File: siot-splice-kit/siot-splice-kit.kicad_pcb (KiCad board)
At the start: 2 copper layers, 40.6 x 46.6 mm, 2 parts, among them J1 xConnect_smd, J2 Screw_Terminal_5mm_01x03

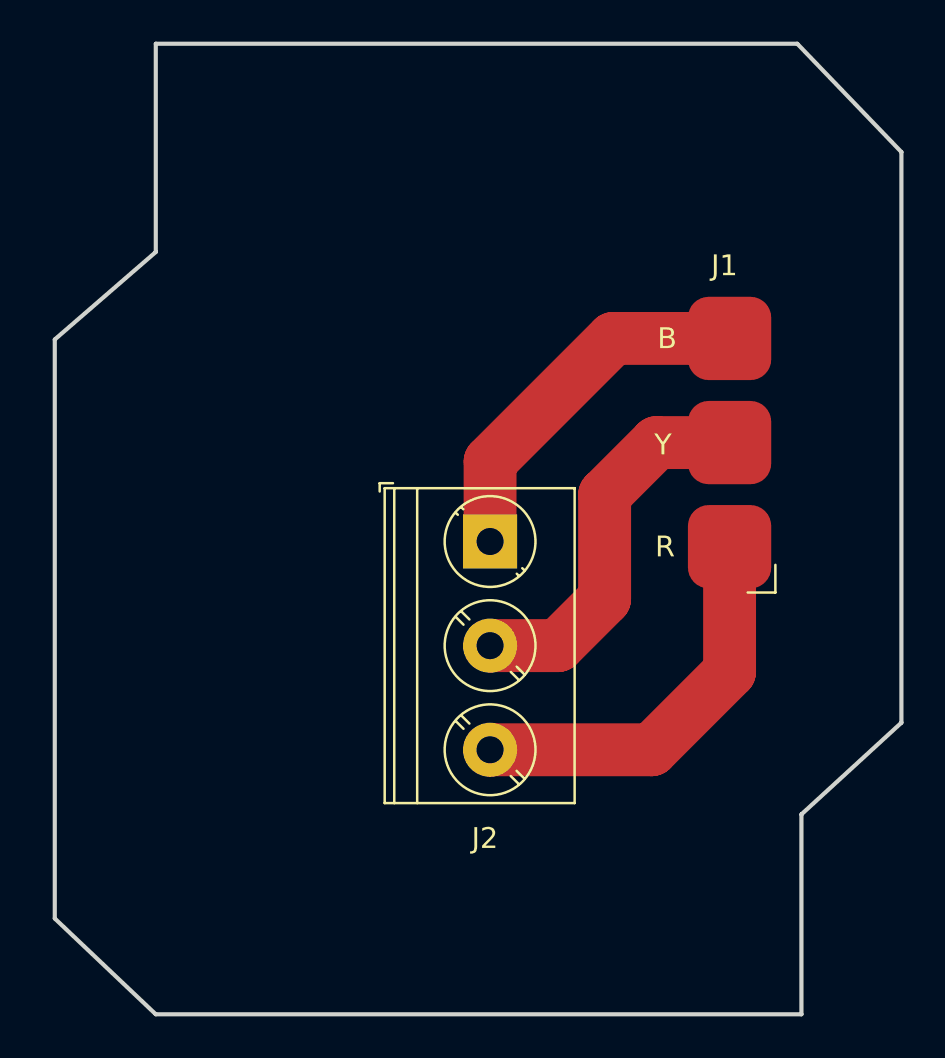
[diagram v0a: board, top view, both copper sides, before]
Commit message: updates for relay/splice kit
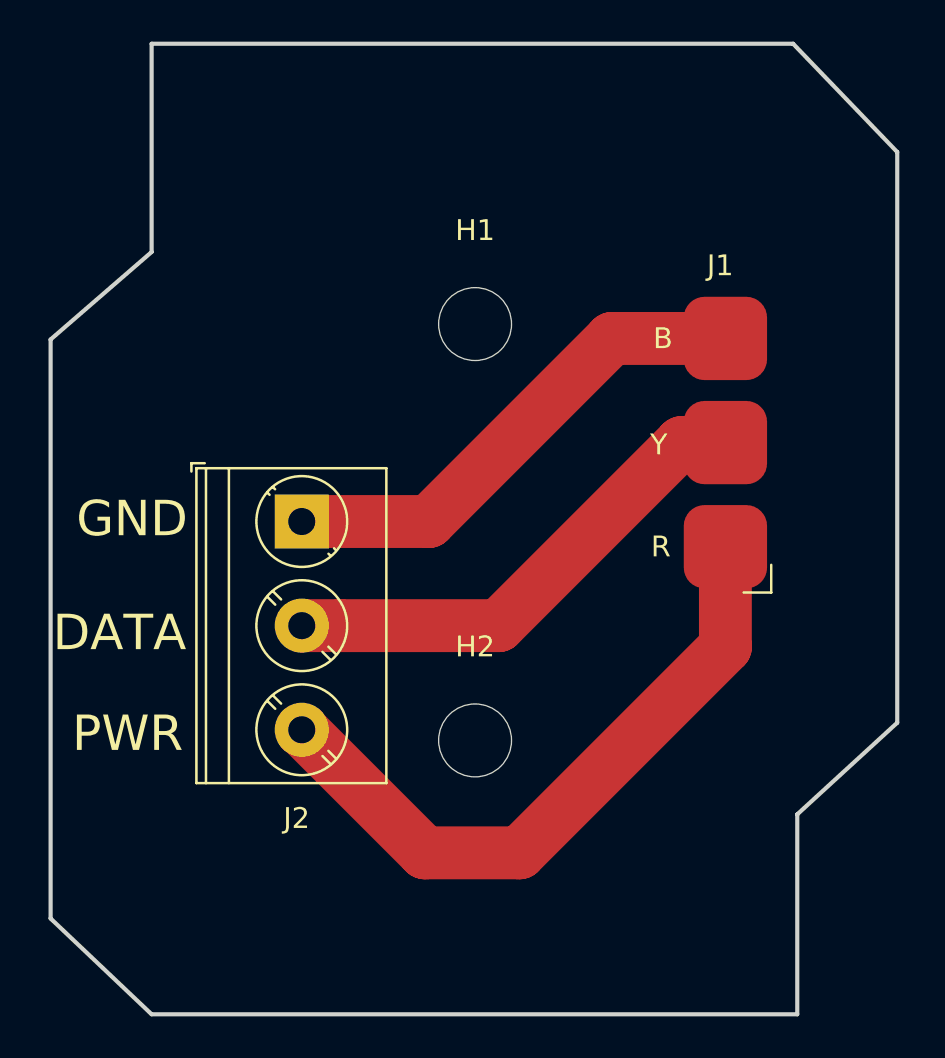
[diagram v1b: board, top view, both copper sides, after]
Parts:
- added H1: MountingHole, MountingHole:MountingHole_3.5mm, F.Cu at (80.3, 75.6)
- added H2: MountingHole, MountingHole:MountingHole_3.5mm, F.Cu at (80.3, 95.5)
- moved J2 9.09 mm to (72.0, 85.0)
- moved J1 0.20 mm to (92.3, 86.2)
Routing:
- net Net-(J1-PadR): track 19.1 -> 31.7 mm
- net Net-(J1-PadB): track 17.8 -> 24.0 mm
- net Net-(J1-PadY): track 18.5 -> 24.0 mm
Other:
- board text added: "DATA"
- board text added: "GND"
- board text added: "PWR"
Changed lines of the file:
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@@
   (general
     (thickness 1.6)
-    (drawings 10)
+    (drawings 35)
     (tracks 11)
     (zones 0)
-    (modules 2)
+    (modules 4)
     (nets 4)
   )
@@
       (outputformat 1)
       (mirror false)
-      (drillshape 1)
+      (drillshape 0)
       (scaleselection 1)
-      (outputdirectory ""))
+      (outputdirectory "mfg/"))
   )
   (net 0 "")
@@
     (add_net "Net-(J1-PadY)")
   )
+  (module MountingHole:MountingHole_3.5mm (layer F.Cu)
+    (at 80.28 95.55)
+    (descr "Mounting Hole 3.5mm, no annular")
+    (tags "mounting hole 3.5mm no annular")
+    (attr virtual)
+    (fp_text reference H2 (at 0 -4.5) (layer F.SilkS)
+      (effects (font (size 1 1) (thickness 0.15)))
+    )
+    (fp_text value MountingHole (at 0 4.5) (layer F.Fab)
+      (effects (font (size 1 1) (thickness 0.15)))
+    )
+    (fp_circle (center 0 0) (end 3.75 0) (layer F.CrtYd) (width 0.05))
+    (fp_circle (center 0 0) (end 3.5 0) (layer Cmts.User) (width 0.15))
+    (fp_text user %R (at 0.3 0) (layer F.Fab)
+      (effects (font (size 1 1) (thickness 0.15)))
+    )
+    (pad 1 np_thru_hole circle (at 0 0) (size 3.5 3.5) (drill 3.5) (layers *.Cu *.Mask))
+  )
+  (module MountingHole:MountingHole_3.5mm (layer F.Cu)
+    (at 80.28 75.56)
+    (descr "Mounting Hole 3.5mm, no annular")
+    (tags "mounting hole 3.5mm no annular")
+    (attr virtual)
+    (fp_text reference H1 (at 0 -4.5) (layer F.SilkS)
+      (effects (font (size 1 1) (thickness 0.15)))
+    )
+    (fp_text value MountingHole (at 0 4.5) (layer F.Fab)
+      (effects (font (size 1 1) (thickness 0.15)))
+    )
+    (fp_circle (center 0 0) (end 3.75 0) (layer F.CrtYd) (width 0.05))
+    (fp_circle (center 0 0) (end 3.5 0) (layer Cmts.User) (width 0.15))
+    (fp_text user %R (at 0.3 0) (layer F.Fab)
+      (effects (font (size 1 1) (thickness 0.15)))
+    )
+    (pad 1 np_thru_hole circle (at 0 0) (size 3.5 3.5) (drill 3.5) (layers *.Cu *.Mask))
+  )
   (module TerminalBlock_Phoenix:TerminalBlock_Phoenix_PT-1,5-3-5.0-H_1x03_P5.00mm_Horizontal (layer F.Cu)
-    (at 81 86 270)
+    (at 71.96 85.04 270)
     (descr "Terminal Block Phoenix PT-1,5-3-5.0-H, 3 pins, pitch 5mm, size 15x9mm^2, drill diamater 1.3mm, pad diameter 2.6mm, see http://www.mouser.com/ds/2/324/ItemDetail_1935161-922578.pdf, script-generated using https://github.com/pointhi/kicad-footprint-generator/scripts/TerminalBlock_Phoenix")
     (tags "THT Terminal Block Phoenix PT-1,5-3-5.0-H pitch 5mm size 15x9mm^2 drill 1.3mm pad 2.6mm")
@@
   )
   (module BEC:xConnect_smd (layer F.Cu)
-    (at 92.5 86.25 180)
+    (at 92.3 86.25 180)
     (descr "mounting holes for xConnect connector")
     (tags "Through hole 1x03 single row")
@@
     )
   )
-  (gr_line (start 100.75 94.7) (end 100.75 67.3) (layer Edge.Cuts) (width 0.2))
-  (gr_line (start 64.95 108.7) (end 95.95 108.7) (layer Edge.Cuts) (width 0.2))
-  (gr_line (start 60.1 76.3) (end 60.1 104.1) (layer Edge.Cuts) (width 0.2))
-  (gr_line (start 95.75 62.1) (end 64.95 62.1) (layer Edge.Cuts) (width 0.2))
-  (gr_line (start 95.75 62.1) (end 100.75 67.3) (layer Edge.Cuts) (width 0.2))
-  (gr_line (start 64.95 62.1) (end 64.95 72.1) (layer Edge.Cuts) (width 0.2))
-  (gr_line (start 64.95 72.1) (end 60.1 76.3) (layer Edge.Cuts) (width 0.2))
-  (gr_line (start 60.1 104.1) (end 64.95 108.7) (layer Edge.Cuts) (width 0.2))
-  (gr_line (start 95.95 108.7) (end 95.95 99.1) (layer Edge.Cuts) (width 0.2))
-  (gr_line (start 95.95 99.1) (end 100.75 94.7) (layer Edge.Cuts) (width 0.2))
-  (segment (start 81 82.16) (end 86.91 76.25) (width 2.54) (layer F.Cu) (net 1))
-  (segment (start 81 86) (end 81 82.16) (width 2.54) (layer F.Cu) (net 1))
-  (segment (start 86.91 76.25) (end 92.5 76.25) (width 2.54) (layer F.Cu) (net 1))
-  (segment (start 81 91) (end 84.25 91) (width 2.54) (layer F.Cu) (net 2))
-  (segment (start 84.25 91) (end 86.5 88.75) (width 2.54) (layer F.Cu) (net 2))
-  (segment (start 86.5 88.75) (end 86.5 83.75) (width 2.54) (layer F.Cu) (net 2))
-  (segment (start 89 81.25) (end 92.5 81.25) (width 2.54) (layer F.Cu) (net 2))
-  (segment (start 86.5 83.75) (end 89 81.25) (width 2.54) (layer F.Cu) (net 2))
-  (segment (start 92.5 92.25) (end 92.5 86.25) (width 2.54) (layer F.Cu) (net 3))
-  (segment (start 81 96) (end 88.75 96) (width 2.54) (layer F.Cu) (net 3))
-  (segment (start 88.75 96) (end 92.5 92.25) (width 2.54) (layer F.Cu) (net 3))
+  (gr_line (start 30.969479 90.248889) (end 30.969479 65.748888) (layer Dwgs.User) (width 0.2))
+  (gr_arc (start 28.875555 56.748889) (end 21.96948 56.748889) (angle -90) (layer Dwgs.User) (width 0.2))
+  (gr_circle (center 5.875555 72.748889) (end 7.590055 72.748889) (layer Dwgs.User) (width 0.2))
+  (gr_arc (start 28.875555 90.248889) (end 28.875555 92.342814) (angle -90) (layer Dwgs.User) (width 0.2))
+  (gr_arc (start 28.875555 99.748889) (end 28.875555 92.342814) (angle -90) (layer Dwgs.User) (width 0.2))
+  (gr_circle (center 5.875555 92.748889) (end 7.590055 92.748889) (layer Dwgs.User) (width 0.2))
+  (gr_line (start 19.875555 54.654965) (end -7.624445 54.654965) (layer Dwgs.User) (width 0.2))
+  (gr_arc (start 19.875555 56.748889) (end 21.96948 56.748889) (angle -90) (layer Dwgs.User) (width 0.2))
+  (gr_line (start 21.46948 108.74889) (end 21.46948 99.74889) (layer Dwgs.User) (width 0.2))
+  (gr_arc (start 19.375555 108.748889) (end 19.375555 110.842814) (angle -90) (layer Dwgs.User) (width 0.2))
+  (gr_line (start -8.124445 110.842814) (end 19.375555 110.842814) (layer Dwgs.User) (width 0.2))
+  (gr_arc (start -17.124445 99.748889) (end -19.21837 99.748889) (angle -90) (layer Dwgs.User) (width 0.2))
+  (gr_line (start -19.218369 75.24889) (end -19.218369 99.74889) (layer Dwgs.User) (width 0.2))
+  (gr_arc (start 28.875555 65.748889) (end 30.96948 65.748889) (angle -90) (layer Dwgs.User) (width 0.2))
+  (gr_line (start -9.71837 56.748889) (end -9.71837 65.748888) (layer Dwgs.User) (width 0.2))
+  (gr_arc (start -7.624445 56.748889) (end -7.624445 54.654965) (angle -90) (layer Dwgs.User) (width 0.2))
+  (gr_arc (start -17.124445 75.248889) (end -17.124445 73.154965) (angle -90) (layer Dwgs.User) (width 0.2))
+  (gr_arc (start -17.124445 108.748889) (end -10.21837 108.748889) (angle -90) (layer Dwgs.User) (width 0.2))
+  (gr_arc (start -17.124445 65.748889) (end -17.124445 73.154965) (angle -90) (layer Dwgs.User) (width 0.2))
+  (gr_arc (start -8.124445 108.748889) (end -10.21837 108.748889) (angle -90) (layer Dwgs.User) (width 0.2))
+  (gr_circle (center 80.275555 75.548889) (end 81.990055 75.548889) (layer Dwgs.User) (width 0.2))
+  (gr_circle (center 80.275555 95.548889) (end 81.990055 95.548889) (layer Dwgs.User) (width 0.2))
+  (gr_text PWR (at 63.6 95.22) (layer F.SilkS)
+    (effects (font (size 1.7 1.7) (thickness 0.25)))
+  )
+  (gr_text DATA (at 63.21 90.38) (layer F.SilkS)
+    (effects (font (size 1.7 1.7) (thickness 0.25)))
+  )
+  (gr_text GND (at 63.81 84.91) (layer F.SilkS)
+    (effects (font (size 1.7 1.7) (thickness 0.25)))
+  )
+  (gr_line (start 100.55 94.7) (end 100.55 67.3) (layer Edge.Cuts) (width 0.2))
+  (gr_line (start 64.75 108.7) (end 95.75 108.7) (layer Edge.Cuts) (width 0.2))
+  (gr_line (start 59.9 76.3) (end 59.9 104.1) (layer Edge.Cuts) (width 0.2))
+  (gr_line (start 95.55 62.1) (end 64.75 62.1) (layer Edge.Cuts) (width 0.2))
+  (gr_line (start 95.55 62.1) (end 100.55 67.3) (layer Edge.Cuts) (width 0.2))
+  (gr_line (start 64.75 62.1) (end 64.75 72.1) (layer Edge.Cuts) (width 0.2))
+  (gr_line (start 64.75 72.1) (end 59.9 76.3) (layer Edge.Cuts) (width 0.2))
+  (gr_line (start 59.9 104.1) (end 64.75 108.7) (layer Edge.Cuts) (width 0.2))
+  (gr_line (start 95.75 108.7) (end 95.75 99.1) (layer Edge.Cuts) (width 0.2))
+  (gr_line (start 95.75 99.1) (end 100.55 94.7) (layer Edge.Cuts) (width 0.2))
+  (segment (start 78.06 85.04) (end 71.96 85.04) (width 2.54) (layer F.Cu) (net 1))
+  (segment (start 92.3 76.25) (end 86.85 76.25) (width 2.54) (layer F.Cu) (net 1))
+  (segment (start 86.85 76.25) (end 78.06 85.04) (width 2.54) (layer F.Cu) (net 1))
+  (segment (start 73.798477 90.04) (end 71.96 90.04) (width 2.54) (layer F.Cu) (net 2))
+  (segment (start 81.41 90.04) (end 73.798477 90.04) (width 2.54) (layer F.Cu) (net 2))
+  (segment (start 90.2 81.25) (end 81.41 90.04) (width 2.54) (layer F.Cu) (net 2))
+  (segment (start 92.3 81.25) (end 90.2 81.25) (width 2.54) (layer F.Cu) (net 2))
+  (segment (start 92.3 86.25) (end 92.3 91.06) (width 2.54) (layer F.Cu) (net 3))
+  (segment (start 92.3 91.06) (end 82.41 100.95) (width 2.54) (layer F.Cu) (net 3))
+  (segment (start 77.87 100.95) (end 71.96 95.04) (width 2.54) (layer F.Cu) (net 3))
+  (segment (start 82.41 100.95) (end 77.87 100.95) (width 2.54) (layer F.Cu) (net 3))
 )

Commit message: updates
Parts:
- moved J2 20.0 mm to (90.6, 92.2)
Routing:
- net Net-(J1-PadR): track 31.7 -> 18.1 mm
- net Net-(J1-PadB): track 24.0 -> 20.9 mm
- net Net-(J1-PadY): track 24.0 -> 23.4 mm, vias 0 -> 1
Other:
- board size 40.6 x 46.6 mm -> 37.3 x 46.6 mm
- board text added: "SIOT Splice Kit v2"
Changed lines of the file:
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@@
   (general
     (thickness 1.6)
-    (drawings 35)
-    (tracks 11)
+    (drawings 36)
+    (tracks 14)
     (zones 0)
     (modules 4)
@@
     (via_min_size 0.4)
     (via_min_drill 0.3)
+    (user_via 2.286 1.016)
     (uvia_size 0.3)
     (uvia_drill 0.1)
@@
   )
   (module TerminalBlock_Phoenix:TerminalBlock_Phoenix_PT-1,5-3-5.0-H_1x03_P5.00mm_Horizontal (layer F.Cu)
-    (at 71.96 85.04 270)
+    (at 90.6 92.2 270)
     (descr "Terminal Block Phoenix PT-1,5-3-5.0-H, 3 pins, pitch 5mm, size 15x9mm^2, drill diamater 1.3mm, pad diameter 2.6mm, see http://www.mouser.com/ds/2/324/ItemDetail_1935161-922578.pdf, script-generated using https://github.com/pointhi/kicad-footprint-generator/scripts/TerminalBlock_Phoenix")
     (tags "THT Terminal Block Phoenix PT-1,5-3-5.0-H pitch 5mm size 15x9mm^2 drill 1.3mm pad 2.6mm")
@@
     )
   )
+  (gr_text "SIOT Splice Kit v2" (at 81 65.2) (layer F.SilkS)
+    (effects (font (size 2 2) (thickness 0.3)))
+  )
   (gr_line (start 30.969479 90.248889) (end 30.969479 65.748888) (layer Dwgs.User) (width 0.2))
   (gr_arc (start 28.875555 56.748889) (end 21.96948 56.748889) (angle -90) (layer Dwgs.User) (width 0.2))
@@
   (gr_circle (center 80.275555 75.548889) (end 81.990055 75.548889) (layer Dwgs.User) (width 0.2))
   (gr_circle (center 80.275555 95.548889) (end 81.990055 95.548889) (layer Dwgs.User) (width 0.2))
-  (gr_text PWR (at 63.6 95.22) (layer F.SilkS)
+  (gr_text PWR (at 72.4 101.6) (layer F.SilkS)
     (effects (font (size 1.7 1.7) (thickness 0.25)))
   )
-  (gr_text DATA (at 63.21 90.38) (layer F.SilkS)
+  (gr_text DATA (at 72.4 96.6) (layer F.SilkS)
     (effects (font (size 1.7 1.7) (thickness 0.25)))
   )
-  (gr_text GND (at 63.81 84.91) (layer F.SilkS)
+  (gr_text GND (at 72.6 92.2) (layer F.SilkS)
     (effects (font (size 1.7 1.7) (thickness 0.25)))
   )
-  (gr_line (start 100.55 94.7) (end 100.55 67.3) (layer Edge.Cuts) (width 0.2))
+  (gr_line (start 98.9 94.7) (end 98.9 67.3) (layer Edge.Cuts) (width 0.2))
   (gr_line (start 64.75 108.7) (end 95.75 108.7) (layer Edge.Cuts) (width 0.2))
-  (gr_line (start 59.9 76.3) (end 59.9 104.1) (layer Edge.Cuts) (width 0.2))
+  (gr_line (start 61.6 76.3) (end 61.6 104.1) (layer Edge.Cuts) (width 0.2))
   (gr_line (start 95.55 62.1) (end 64.75 62.1) (layer Edge.Cuts) (width 0.2))
-  (gr_line (start 95.55 62.1) (end 100.55 67.3) (layer Edge.Cuts) (width 0.2))
+  (gr_line (start 95.55 62.1) (end 98.9 67.3) (layer Edge.Cuts) (width 0.2))
   (gr_line (start 64.75 62.1) (end 64.75 72.1) (layer Edge.Cuts) (width 0.2))
-  (gr_line (start 64.75 72.1) (end 59.9 76.3) (layer Edge.Cuts) (width 0.2))
-  (gr_line (start 59.9 104.1) (end 64.75 108.7) (layer Edge.Cuts) (width 0.2))
+  (gr_line (start 64.75 72.1) (end 61.6 76.3) (layer Edge.Cuts) (width 0.2))
+  (gr_line (start 61.6 104.1) (end 64.75 108.7) (layer Edge.Cuts) (width 0.2))
   (gr_line (start 95.75 108.7) (end 95.75 99.1) (layer Edge.Cuts) (width 0.2))
-  (gr_line (start 95.75 99.1) (end 100.55 94.7) (layer Edge.Cuts) (width 0.2))
-  (segment (start 78.06 85.04) (end 71.96 85.04) (width 2.54) (layer F.Cu) (net 1))
-  (segment (start 92.3 76.25) (end 86.85 76.25) (width 2.54) (layer F.Cu) (net 1))
-  (segment (start 86.85 76.25) (end 78.06 85.04) (width 2.54) (layer F.Cu) (net 1))
-  (segment (start 73.798477 90.04) (end 71.96 90.04) (width 2.54) (layer F.Cu) (net 2))
-  (segment (start 81.41 90.04) (end 73.798477 90.04) (width 2.54) (layer F.Cu) (net 2))
-  (segment (start 90.2 81.25) (end 81.41 90.04) (width 2.54) (layer F.Cu) (net 2))
-  (segment (start 92.3 81.25) (end 90.2 81.25) (width 2.54) (layer F.Cu) (net 2))
-  (segment (start 92.3 86.25) (end 92.3 91.06) (width 2.54) (layer F.Cu) (net 3))
-  (segment (start 92.3 91.06) (end 82.41 100.95) (width 2.54) (layer F.Cu) (net 3))
-  (segment (start 77.87 100.95) (end 71.96 95.04) (width 2.54) (layer F.Cu) (net 3))
-  (segment (start 82.41 100.95) (end 77.87 100.95) (width 2.54) (layer F.Cu) (net 3))
+  (gr_line (start 95.75 99.1) (end 98.9 94.7) (layer Edge.Cuts) (width 0.2))
+  (segment (start 90.2 76.25) (end 87 79.45) (width 2.54) (layer F.Cu) (net 1))
+  (segment (start 92.3 76.25) (end 90.2 76.25) (width 2.54) (layer F.Cu) (net 1))
+  (segment (start 87 88.6) (end 90.6 92.2) (width 2.54) (layer F.Cu) (net 1))
+  (segment (start 87 79.45) (end 87 88.6) (width 2.54) (layer F.Cu) (net 1))
+  (via (at 96.1 81.2) (size 2.286) (drill 1.016) (layers F.Cu B.Cu) (net 2))
+  (segment (start 92.3 81.25) (end 96.05 81.25) (width 2.54) (layer F.Cu) (net 2))
+  (segment (start 96.05 81.25) (end 96.1 81.2) (width 2.54) (layer F.Cu) (net 2))
+  (segment (start 96.1 81.2) (end 96.1 93.9) (width 2.54) (layer B.Cu) (net 2))
+  (segment (start 92.8 97.2) (end 90.6 97.2) (width 2.54) (layer B.Cu) (net 2))
+  (segment (start 96.1 93.9) (end 92.8 97.2) (width 2.54) (layer B.Cu) (net 2))
+  (segment (start 94 90.05) (end 94 98.8) (width 2.54) (layer F.Cu) (net 3))
+  (segment (start 92.3 88.35) (end 94 90.05) (width 2.54) (layer F.Cu) (net 3))
+  (segment (start 94 98.8) (end 90.6 102.2) (width 2.54) (layer F.Cu) (net 3))
+  (segment (start 92.3 86.25) (end 92.3 88.35) (width 2.54) (layer F.Cu) (net 3))
 )
